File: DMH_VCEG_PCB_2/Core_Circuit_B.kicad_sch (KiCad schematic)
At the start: 84 parts, among them J25 Conn_01x10_PinHeader, Q5 BC548, Q6 BC558, Q7 BC548, SW2 SW_DPDT_x2, U10 TL074, U11 4001, U12 40106, U13 CD4066BE, U14 TL074, U15 TL074, U16 TL074

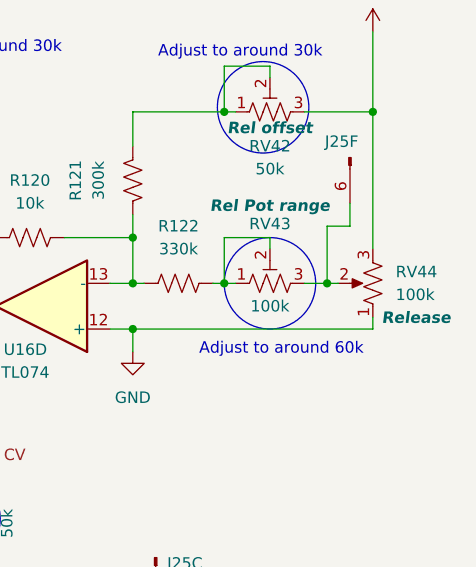
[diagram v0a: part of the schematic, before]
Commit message: Placed front panel components on PCB 2
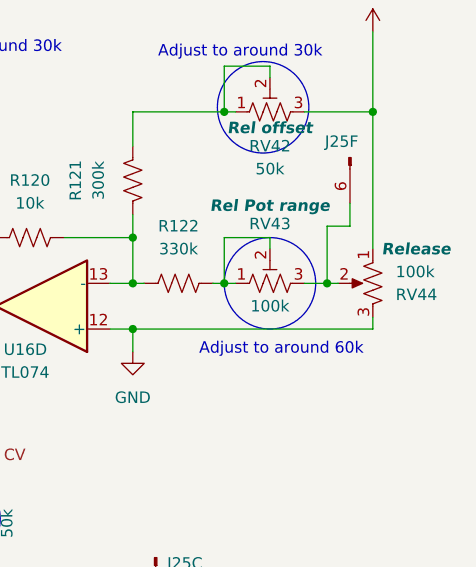
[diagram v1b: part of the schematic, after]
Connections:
- net +12V: now also RV44.1; no longer RV44.3
- net GND: now also RV44.3; no longer RV44.1
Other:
- moved on the sheet: RV44

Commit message: Placed ICs and pin headers on PCB 2
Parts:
- J25: footprint (none) -> Connector_PinSocket_2.54mm:PinSocket_1x10_P2.54mm_Vertical
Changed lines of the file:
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@@
 			)
 		)
-		(property "Footprint" ""
+		(property "Footprint" "Connector_PinSocket_2.54mm:PinSocket_1x10_P2.54mm_Vertical"
 			(at 184.15 139.7 0)
 			(effects
@@
 			)
 		)
-		(property "Footprint" ""
+		(property "Footprint" "Connector_PinSocket_2.54mm:PinSocket_1x10_P2.54mm_Vertical"
 			(at 273.05 33.02 0)
 			(effects
@@
 		(exclude_from_sim no)
 		(in_bom yes)
-		(on_board yes)
+		(on_board no)
 		(dnp no)
 		(property "Reference" "U10"
@@
 			)
 		)
-		(property "Footprint" ""
+		(property "Footprint" "Connector_PinSocket_2.54mm:PinSocket_1x10_P2.54mm_Vertical"
 			(at 127 157.48 0)
 			(effects
@@
 			)
 		)
-		(property "Footprint" ""
+		(property "Footprint" "Connector_PinSocket_2.54mm:PinSocket_1x10_P2.54mm_Vertical"
 			(at 151.13 189.23 0)
 			(effects
@@
 		(exclude_from_sim no)
 		(in_bom yes)
-		(on_board yes)
+		(on_board no)
 		(dnp no)
 		(property "Reference" "U10"
@@
 			)
 		)
-		(property "Footprint" ""
+		(property "Footprint" "Connector_PinSocket_2.54mm:PinSocket_1x10_P2.54mm_Vertical"
 			(at 251.46 77.47 0)
 			(effects

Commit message: Added Output attenuation circuit
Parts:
- RV34, RV40, RV44: value 100k -> C100k
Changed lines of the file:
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@@
 			)
 		)
-		(property "Value" "100k"
+		(property "Value" "C100k"
 			(at 132.08 166.3701 0)
 			(effects
@@
 			)
 		)
-		(property "Value" "100k"
+		(property "Value" "C100k"
 			(at 260.35 95.2499 0)
 			(effects
@@
 			)
 		)
-		(property "Value" "100k"
+		(property "Value" "C100k"
 			(at 278.13 45.7201 0)
 			(effects

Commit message: Removed unnecessary trimpots
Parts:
- removed RV31, RV37, RV38: 50k, Potentiometer_THT:Potentiometer_Bourns_3296W_Vertical, symbol Device:R_Potentiometer_Trim_US
- removed RV33, RV39, RV43: 100k, Potentiometer_THT:Potentiometer_Bourns_3296W_Vertical, symbol Device:R_Potentiometer_Trim_US
- R100, R119, R122: value 330k -> 390k
- R116, R118, R92: value 470k -> 499k
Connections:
- net Att CV: now also R118.2
- net Dec CV: now also R92.2
- net Rel CV: now also R116.2
- net at R122.1: now also J25.6 (Pin_6), RV44.2
- net at R100.1: now also J25.4 (Pin_4), RV34.2
- net at R119.1: now also J25.3 (Pin_3), RV40.2
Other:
- note removed: "Adjust to around 60k"
- moved on the sheet: R119, R122

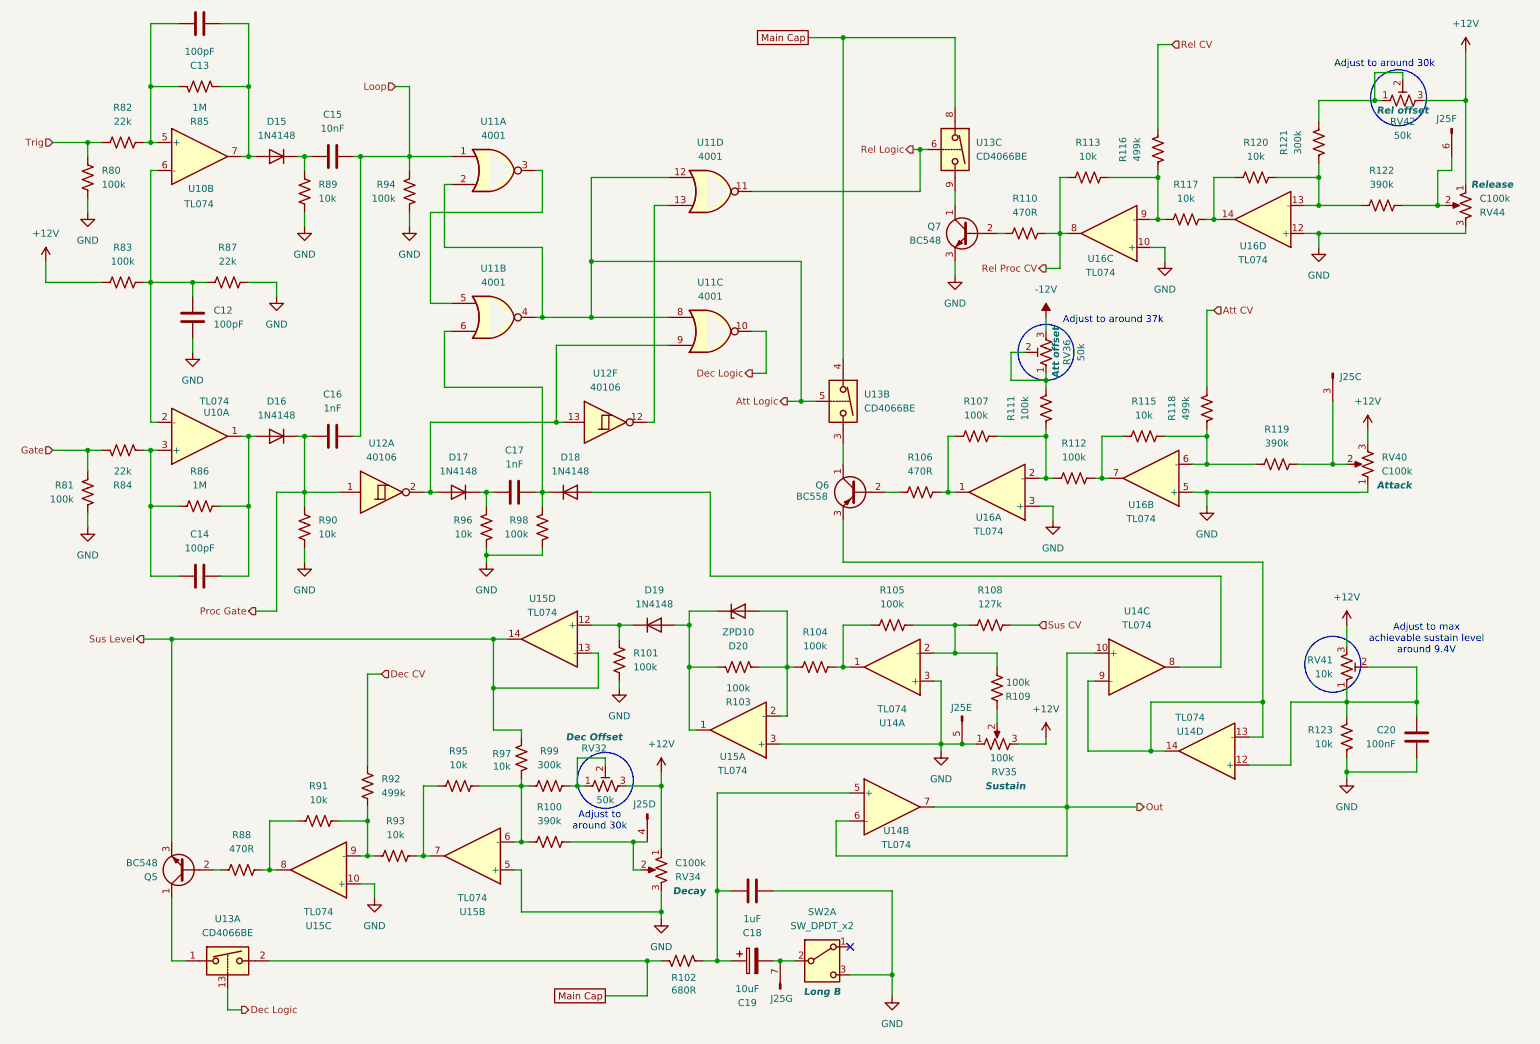
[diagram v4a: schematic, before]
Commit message: Synced PCB 2 project with PCB 1
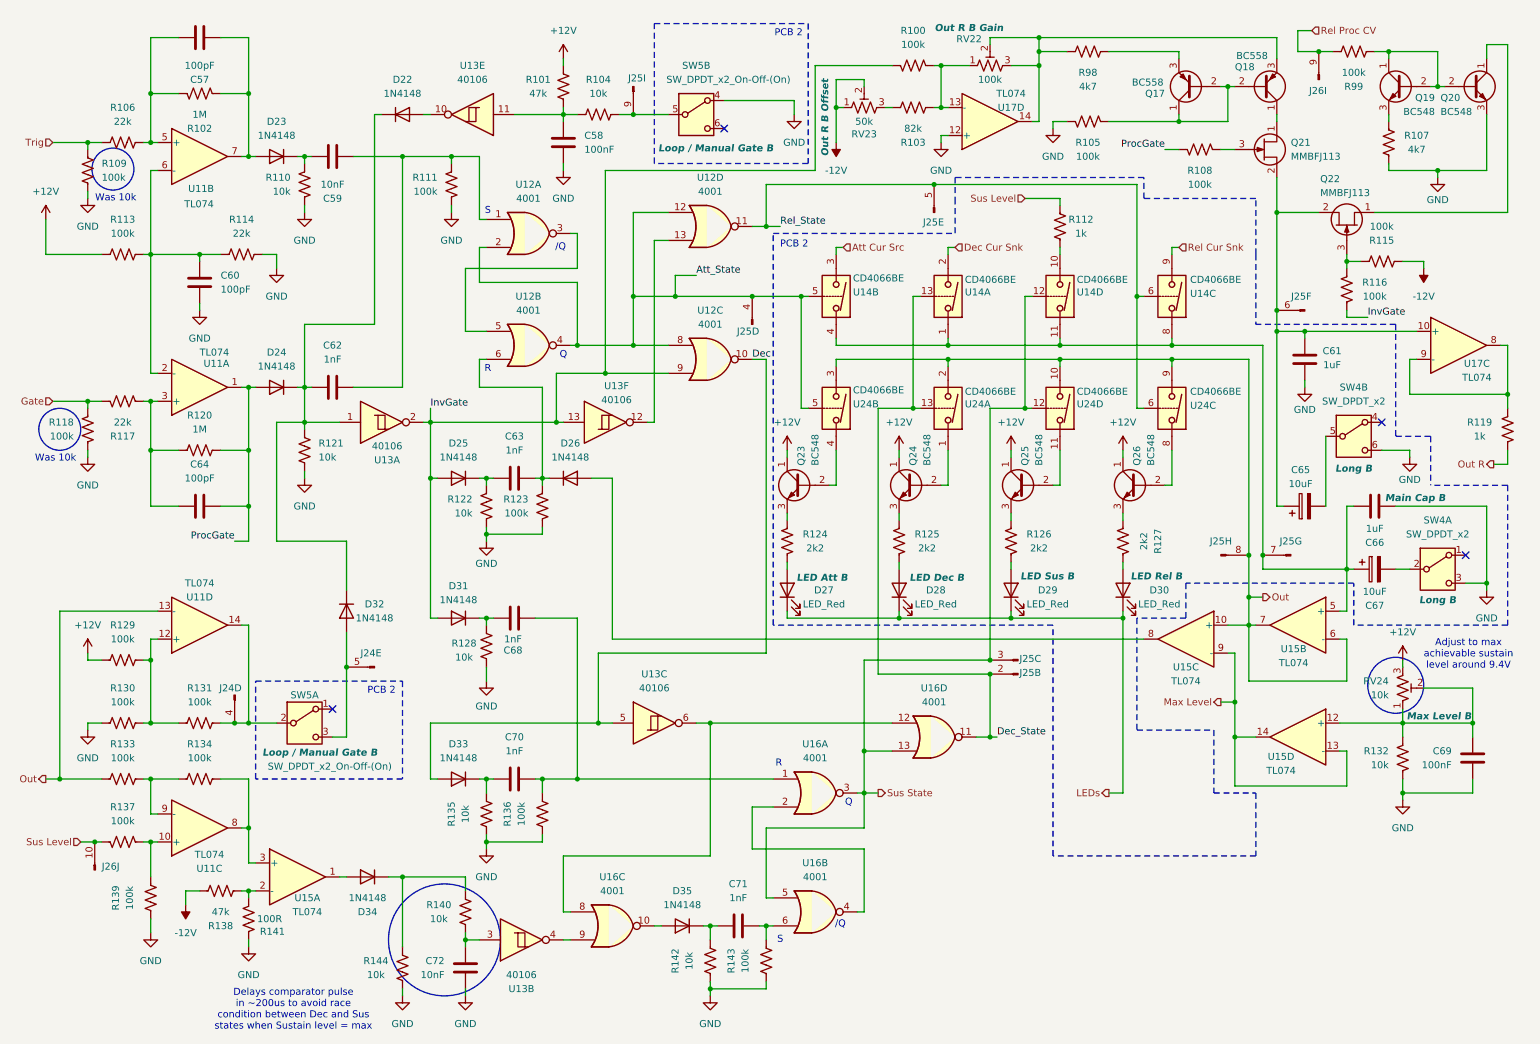
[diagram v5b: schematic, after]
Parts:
- removed C12, C13, C14: 100pF, Capacitor_THT:C_Disc_D3.8mm_W2.6mm_P2.50mm, symbol Device:C
- removed C15: 10nF, Capacitor_THT:C_Disc_D4.3mm_W1.9mm_P5.00mm, symbol Device:C
- removed C16, C17: 1nF, Capacitor_THT:C_Disc_D4.3mm_W1.9mm_P5.00mm, symbol Device:C
- removed C18: 1uF, Capacitor_THT:C_Disc_D4.3mm_W1.9mm_P5.00mm, symbol Device:C
- removed C19: 10uF, Capacitor_THT:CP_Radial_D5.0mm_P2.00mm, symbol Device:C_Polarized
- removed C20: 100nF, Capacitor_THT:C_Disc_D4.3mm_W1.9mm_P5.00mm, symbol Device:C
- removed D15, D16, D17, D18, D19: 1N4148, Diode_THT:D_DO-35_SOD27_P7.62mm_Horizontal, symbol Diode:1N4148
- removed D20: ZPD10, Diode_THT:D_DO-35_SOD27_P7.62mm_Horizontal, symbol Diode:ZPDxx
- removed Q5, Q7: BC548, Package_TO_SOT_THT:TO-92L_Inline_Wide, symbol Transistor_BJT:BC548
- removed Q6: BC558, Package_TO_SOT_THT:TO-92L_Inline_Wide, symbol Transistor_BJT:BC558
- removed R80, R81, R83, R94: 100k, Resistor_THT:R_Axial_DIN0207_L6.3mm_D2.5mm_P7.62mm_Horizontal, symbol Device:R_US
- removed R82, R84, R87: 22k, Resistor_THT:R_Axial_DIN0207_L6.3mm_D2.5mm_P7.62mm_Horizontal, symbol Device:R_US
- removed R85, R86: 1M, Resistor_THT:R_Axial_DIN0207_L6.3mm_D2.5mm_P7.62mm_Horizontal, symbol Device:R_US
- removed R88: 470R, Resistor_THT:R_Axial_DIN0207_L6.3mm_D2.5mm_P7.62mm_Horizontal, symbol Device:R_US
- removed R89, R90, R91, R93, R95, R96, R97: 10k, Resistor_THT:R_Axial_DIN0207_L6.3mm_D2.5mm_P7.62mm_Horizontal, symbol Device:R_US
- removed R92: 499k, Resistor_THT:R_Axial_DIN0207_L6.3mm_D2.5mm_P7.62mm_Horizontal, symbol Device:R_US
- removed RV32, RV36, RV42: 50k, Potentiometer_THT:Potentiometer_Bourns_3296W_Vertical, symbol Device:R_Potentiometer_Trim_US
- removed RV34, RV40, RV44: C100k, SynthStuff:Potentiometer_Alpha_RD901F-40-00D_Single_Vertical, symbol Device:R_Potentiometer_US
- removed RV35: 100k, SynthStuff:Potentiometer_Alpha_RD901F-40-00D_Single_Vertical, symbol Device:R_Potentiometer_US
- removed RV41: 10k, Potentiometer_THT:Potentiometer_Bourns_3296W_Vertical, symbol Device:R_Potentiometer_Trim_US
- removed SW2: SW_DPDT_x2, SynthStuff:Toggle_Switch_2_Poles_TE, symbol Switch:SW_DPDT_x2
- removed U10, U14, U16: TL074, Package_DIP:DIP-14_W7.62mm_Socket, symbol Amplifier_Operational:TL074
- removed U11: 4001, Package_DIP:DIP-14_W7.62mm_Socket, symbol 4xxx:4001
- removed U12: 40106, Package_DIP:DIP-14_W7.62mm_Socket, symbol 4xxx:40106
- removed U13: CD4066BE, Package_DIP:DIP-14_W7.62mm, symbol Analog_Switch:CD4066BE
- added C57, C60, C64: 100pF, Capacitor_THT:C_Disc_D3.8mm_W2.6mm_P2.50mm, symbol Device:C
- added C58, C69: 100nF, Capacitor_THT:C_Disc_D4.3mm_W1.9mm_P5.00mm, symbol Device:C
- added C59, C72: 10nF, Capacitor_THT:C_Disc_D4.3mm_W1.9mm_P5.00mm, symbol Device:C
- added C61, C66: 1uF, Capacitor_THT:C_Rect_L7.0mm_W4.5mm_P5.00mm, symbol Device:C
- added C62, C63, C68, C70, C71: 1nF, Capacitor_THT:C_Disc_D4.3mm_W1.9mm_P5.00mm, symbol Device:C
- added C65, C67: 10uF, Capacitor_THT:CP_Radial_D4.0mm_P1.50mm, symbol Device:C_Polarized
- added D22, D23, D24, D25, D26, D31, D32, D33, D34, D35: 1N4148, Diode_THT:D_DO-35_SOD27_P7.62mm_Horizontal, symbol Diode:1N4148
- added D27, D28, D29, D30: LED_Red, LED_THT:LED_D3.0mm, symbol Device:LED
- added J24: Conn_01x06_PinHeader, Connector_PinHeader_2.54mm:PinHeader_1x06_P2.54mm_Vertical, symbol SynthStuff:Conn_01x06_PinHeader
- added unit 2 of J25
- added unit 9 of J25
- added unit 8 of J25
- added J26: Conn_01x10_PinHeader, Connector_PinSocket_2.54mm:PinSocket_1x10_P2.54mm_Vertical, symbol SynthStuff:Conn_01x10_PinHeader
- added Q17, Q18: BC558, Package_TO_SOT_THT:TO-92L_Inline_Wide, symbol Transistor_BJT:BC558
- added Q19, Q20, Q23, Q24, Q25, Q26: BC548, Package_TO_SOT_THT:TO-92L_Inline_Wide, symbol Transistor_BJT:BC548
- added Q21, Q22: MMBFJ113, Package_TO_SOT_THT:TO-92L_Inline, symbol Transistor_FET:MMBFJ113
- added R114: 22k, Resistor_THT:R_Axial_DIN0207_L6.3mm_D2.5mm_P7.62mm_Horizontal, symbol Device:R_US
- added R124, R125, R126, R127: 2k2, Resistor_THT:R_Axial_DIN0207_L6.3mm_D2.5mm_P7.62mm_Horizontal, symbol Device:R_US
- added R128, R132, R135, R140, R142, R144: 10k, Resistor_THT:R_Axial_DIN0207_L6.3mm_D2.5mm_P7.62mm_Horizontal, symbol Device:R_US
- added R129, R130, R131, R133, R134, R136, R137, R139, R143: 100k, Resistor_THT:R_Axial_DIN0207_L6.3mm_D2.5mm_P7.62mm_Horizontal, symbol Device:R_US
- added R138: 47k, Resistor_THT:R_Axial_DIN0207_L6.3mm_D2.5mm_P7.62mm_Horizontal, symbol Device:R_US
- added R141: 100R, Resistor_THT:R_Axial_DIN0207_L6.3mm_D2.5mm_P7.62mm_Horizontal, symbol Device:R_US
- added RV22: 100k, Potentiometer_THT:Potentiometer_Bourns_3296W_Vertical, symbol Device:R_Potentiometer_Trim_US
- added RV23: 50k, Potentiometer_THT:Potentiometer_Bourns_3296W_Vertical, symbol Device:R_Potentiometer_Trim_US
- added RV24: 10k, Potentiometer_THT:Potentiometer_Bourns_3296W_Vertical, symbol Device:R_Potentiometer_Trim_US
- added SW4: SW_DPDT_x2, SynthStuff:Toggle_Switch_2_Poles_TE, symbol Switch:SW_DPDT_x2
- added SW5: SW_DPDT_x2_On-Off-(On), SynthStuff:Toggle_Switch_2_Poles_TE, symbol Switch:SW_DPDT_x2
- added U11, U17: TL074, Package_DIP:DIP-14_W7.62mm_Socket, symbol Amplifier_Operational:TL074
- added U12, U16: 4001, Package_DIP:DIP-14_W7.62mm_Socket, symbol 4xxx:4001
- added U13: 40106, Package_DIP:DIP-14_W7.62mm_Socket, symbol 4xxx:40106
- added U14, U24: CD4066BE, Package_DIP:DIP-14_W7.62mm, symbol Analog_Switch:CD4066BE
- J25: footprint Connector_PinSocket_2.54mm:PinSocket_1x10_P2.54mm_Vertical -> Connector_PinHeader_2.54mm:PinHeader_1x10_P2.54mm_Vertical
- R100: value 390k -> 100k
- R101: value 100k -> 47k
- R102: value 680R -> 1M
- R103: value 100k -> 82k
- R104: value 100k -> 10k
- R106: value 470R -> 22k
- R107, R98: value 100k -> 4k7
- R108: value 127k -> 100k
- R110: value 470R -> 10k
- R112: value 100k -> 1k
- R113, R115, R123: value 10k -> 100k
- R116, R118: value 499k -> 100k
- R117: value 10k -> 22k
- R119: value 390k -> 1k
- R120: value 10k -> 1M
- R121: value 300k -> 10k
- R122: value 390k -> 10k
- R99: value 300k -> 100k
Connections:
- net Att CV is gone; now on net Gate: R118.2
- net +12V: now also R101.1, R113.2, Q23.1 (C), Q24.1 (C), Q25.1 (C), Q26.1 (C), R129.2, RV24.3
- net -12V: now also R115.1, R138.1, RV23.1, RV23.2
- net GND: now also R105.2, R107.1, R109.1, R110.1, R111.1, R118.1, R121.1, R122.1, C58.2, C60.1, C61.1, C66.2, C69.1, C72.1, Q20.3 (E), R114.1, R128.2, R130.2, R132.1, R135.2, R136.2, R139.2, R141.2, R142.2, R143.2, R144.2, SW4.3 (C), SW4.6 (C), SW5.4 (A), U17.12 (+); no longer J25.5 (Pin_5), R101.1, R98.1, U15.10 (+), U15.3 (+), U15.5 (+)
- net Gate: now also R117.2
- net Out: now also U15.10 (+), U15.6 (-), U15.7, J25.8 (Pin_8), R133.2, U11.13 (-), U24.10, U24.2, U24.3, U24.9
- net Rel Proc CV: now also R99.1, J26.9 (Pin_9); no longer R110.1, R113.2
- net Sus Level: now also R112.2, J26.10 (Pin_10), R137.1; no longer U15.13 (-), U15.14
- net Trig: now also R106.2, R109.2
- net at R123.2: now also C63.2, D26.1 (K), U12.6
- net Att_State: now reaches J25.4 (Pin_4)
- net Att_State: now also U12.12, U12.2, U12.4, U12.8, U14.5, U24.5; no longer R100.1
- net at R102.1: now also C57.2, D23.2 (A), U11.7
- net Max Level: now reaches U15.9 (-)
- net Max Level: now also U15.13 (-), U15.14
- net at R107.2: now also Q19.3 (E); no longer R106.1
- net at R110.2: now also C59.1, D23.1 (K)
- net at U15.8: now also D26.2 (A)
- net at J25.6 (Pin_6): now also C61.2, C65.1, Q21.2 (S), Q22.2 (S), U17.10 (+); no longer R122.1
- net at R115.2: now also R116.1, Q22.3 (G); no longer R112.1
- net at R101.2: now also R104.2, C58.1, U13.11; no longer U15.12 (+)
- net at R103.2: now also R100.2, RV22.1, U17.13 (-); no longer U15.1
- net at R98.2: now also Q17.3 (E)
- net at R121.2: now also C62.1, D22.1 (K), D24.1 (K), D32.1 (K), U13.1
- net at J25.7 (Pin_7): now also U15.5 (+), C66.1, C67.1, U14.1, U14.11, U14.4, U14.8
- net at R111.2: now also C59.2, C62.2, U12.1
- net at R117.1, R120.2: now also C64.1, U11.3 (+)
- net at R104.1: now also J25.9 (Pin_9), SW5.5 (B); no longer R105.2
- net Out R: now reaches R119.1
- net Out R: no longer J25.3 (Pin_3)
- net Main Cap: no longer names the net of R102.2
- net Main Cap: now also R106.1, C57.1, U11.5 (+)
- net Rel CV renamed InvGate
- net InvGate: now also R100.1, D25.2 (A), D31.2 (A), U12.9, U13.13, U13.2
- net Sus CV: no longer names the net of R108.1
- net Sus CV: now also Q21.3 (G)
- new net: Q23.2 (B), U24.4
- new net: Q26.3 (E), R127.1
- new net: D30.2 (A), R127.2
- new net: D32.2 (A), J24.5 (Pin_5), SW5.3 (C)
- new net: C63.1, D25.1 (K), R122.2
- new net: Q25.2 (B), U24.11
- new net: C65.2, SW4.5 (B)
- new net: C60.2, R113.1, R114.2, U11.2 (-), U11.6 (-)
- new net: Q20.1 (C), Q22.1 (D)
- new net: Q26.2 (B), U24.8
- new net: R137.2, R139.1, U11.10 (+)
- new net: R134.1, U11.8, U15.3 (+)
- new net: R133.1, R134.2, U11.9 (-)
- new net: D22.2 (A), U13.10
- new net: U12.3, U12.5
- new net: Q25.3 (E), R126.1
- new net: Q23.3 (E), R124.1
- new net: D27.2 (A), R124.2
- new net: U12.13, U13.12
- new net: Q18.1 (C), Q21.1 (D)
- new net: C69.2, R132.2, RV24.1, RV24.2, U15.12 (+)
- new net: Q19.1 (C), Q19.2 (B), Q20.2 (B), R99.2
- new net: Q24.3 (E), R125.1
- new net: D28.2 (A), R125.2
- new net: Q18.3 (E), R98.1, RV22.2, RV22.3, U17.14
- new net: R112.1, U14.10
- new net: C68.1, D31.1 (K), R128.1
- new net: C68.2, C70.2, R136.1, U16.1
- new net: U13.6, U16.12, U16.8
- new net: D29.2 (A), R126.2
- new net: J24.4 (Pin_4), R131.1, SW5.2 (B), U11.14
- new net: D34.2 (A), U15.1
- new net: R138.2, R141.1, U15.2 (-)
- new net: C71.1, D35.1 (K), R142.1
- new net: Q17.1 (C), Q17.2 (B), Q18.2 (B), R105.1
- new net: C70.1, D33.1 (K), R135.1
- new net: U16.2, U16.4
- new net: D35.2 (A), U16.10
- new net: U13.4, U16.9
- new net: R119.2, U17.8, U17.9 (-)
- new net: R129.1, R130.1, R131.2, U11.12 (+)
- new net: D34.1 (K), R140.1, R144.1
- new net: C72.2, R140.2, U13.3
- new net: C67.2, SW4.2 (B)
- new net: C71.2, R143.1, U16.6
- new net: Q24.2 (B), U24.1
- new net: R103.1, RV23.3
- new net Att Cur Src: U14.3
- new net Dec: D33.2 (A), U12.10, U13.5
- new net Dec Cur Snk: U14.2
- new net Dec_State: J25.2 (Pin_2), U14.13, U16.11, U24.13
- new net LEDs: D27.1 (K), D28.1 (K), D29.1 (K), D30.1 (K)
- new net ProcGate: C64.2, D24.2 (A), R108.2, R120.1, U11.1
- new net Rel Cur Snk: U14.9
- new net Rel_State: J25.5 (Pin_5), U12.11, U14.6, U24.6
- new net Sus State: J25.3 (Pin_3), U14.12, U16.13, U16.3, U16.5, U24.12
- no-connect marks 1 -> 4
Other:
- note added: "/Q"
- note added: "Delays comparator pulse in ~200us to avoid race condition between Dec and Sus states when Sustain level = max"
- note added: "PCB 2"
- note added: "Q"
- note added: "R"
- note added: "S"
- note added: "Was 10k"
- note removed: "Adjust to around 30k"
- note removed: "Adjust to around 37k"

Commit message: Started placement on PCB 2
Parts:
- J24: footprint Connector_PinHeader_2.54mm:PinHeader_1x06_P2.54mm_Vertical -> Connector_PinSocket_2.54mm:PinSocket_1x06_P2.54mm_Vertical
- J25: footprint Connector_PinHeader_2.54mm:PinHeader_1x10_P2.54mm_Vertical -> Connector_PinSocket_2.54mm:PinSocket_1x10_P2.54mm_Vertical
- U14, U24: footprint Package_DIP:DIP-14_W7.62mm -> Package_DIP:DIP-14_W7.62mm_Socket
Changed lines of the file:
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@@
 			)
 		)
-		(property "Footprint" "Package_DIP:DIP-14_W7.62mm"
+		(property "Footprint" "Package_DIP:DIP-14_W7.62mm_Socket"
 			(at 158.75 83.82 0)
 			(effects
@@
 			)
 		)
-		(property "Footprint" "Package_DIP:DIP-14_W7.62mm"
+		(property "Footprint" "Package_DIP:DIP-14_W7.62mm_Socket"
 			(at 199.39 83.82 0)
 			(effects
@@
 			)
 		)
-		(property "Footprint" "Package_DIP:DIP-14_W7.62mm"
+		(property "Footprint" "Package_DIP:DIP-14_W7.62mm_Socket"
 			(at 219.71 83.82 0)
 			(effects
@@
 			)
 		)
-		(property "Footprint" "Connector_PinHeader_2.54mm:PinHeader_1x10_P2.54mm_Vertical"
+		(property "Footprint" "Connector_PinSocket_2.54mm:PinSocket_1x10_P2.54mm_Vertical"
 			(at 179.07 48.26 0)
 			(effects
@@
 			)
 		)
-		(property "Footprint" "Connector_PinHeader_2.54mm:PinHeader_1x06_P2.54mm_Vertical"
+		(property "Footprint" "Connector_PinSocket_2.54mm:PinSocket_1x06_P2.54mm_Vertical"
 			(at 77.47 130.81 0)
 			(effects
@@
 			)
 		)
-		(property "Footprint" "Package_DIP:DIP-14_W7.62mm"
+		(property "Footprint" "Package_DIP:DIP-14_W7.62mm_Socket"
 			(at 158.75 63.5 0)
 			(effects
@@
 			)
 		)
-		(property "Footprint" "Connector_PinHeader_2.54mm:PinHeader_1x06_P2.54mm_Vertical"
+		(property "Footprint" "Connector_PinSocket_2.54mm:PinSocket_1x06_P2.54mm_Vertical"
 			(at 52.07 135.89 0)
 			(effects
@@
 			)
 		)
-		(property "Footprint" "Connector_PinHeader_2.54mm:PinHeader_1x10_P2.54mm_Vertical"
+		(property "Footprint" "Connector_PinSocket_2.54mm:PinSocket_1x10_P2.54mm_Vertical"
 			(at 194.31 132.08 0)
 			(effects
@@
 			)
 		)
-		(property "Footprint" "Connector_PinHeader_2.54mm:PinHeader_1x10_P2.54mm_Vertical"
+		(property "Footprint" "Connector_PinSocket_2.54mm:PinSocket_1x10_P2.54mm_Vertical"
 			(at 194.31 129.54 0)
 			(effects
@@
 			)
 		)
-		(property "Footprint" "Package_DIP:DIP-14_W7.62mm"
+		(property "Footprint" "Package_DIP:DIP-14_W7.62mm_Socket"
 			(at 179.07 63.5 0)
 			(effects
@@
 			)
 		)
-		(property "Footprint" "Connector_PinHeader_2.54mm:PinHeader_1x10_P2.54mm_Vertical"
+		(property "Footprint" "Connector_PinSocket_2.54mm:PinSocket_1x10_P2.54mm_Vertical"
 			(at 124.46 25.4 0)
 			(effects
@@
 			)
 		)
-		(property "Footprint" "Package_DIP:DIP-14_W7.62mm"
+		(property "Footprint" "Package_DIP:DIP-14_W7.62mm_Socket"
 			(at 219.71 63.5 0)
 			(effects
@@
 			)
 		)
-		(property "Footprint" "Package_DIP:DIP-14_W7.62mm"
+		(property "Footprint" "Package_DIP:DIP-14_W7.62mm_Socket"
 			(at 179.07 83.82 0)
 			(effects
@@
 			)
 		)
-		(property "Footprint" "Connector_PinHeader_2.54mm:PinHeader_1x10_P2.54mm_Vertical"
+		(property "Footprint" "Connector_PinSocket_2.54mm:PinSocket_1x10_P2.54mm_Vertical"
 			(at 146.05 68.58 0)
 			(effects
@@
 			)
 		)
-		(property "Footprint" "Connector_PinHeader_2.54mm:PinHeader_1x10_P2.54mm_Vertical"
+		(property "Footprint" "Connector_PinSocket_2.54mm:PinSocket_1x10_P2.54mm_Vertical"
 			(at 246.38 66.04 0)
 			(effects
@@
 			)
 		)
-		(property "Footprint" "Connector_PinHeader_2.54mm:PinHeader_1x10_P2.54mm_Vertical"
+		(property "Footprint" "Connector_PinSocket_2.54mm:PinSocket_1x10_P2.54mm_Vertical"
 			(at 231.14 110.49 0)
 			(effects
@@
 			)
 		)
-		(property "Footprint" "Package_DIP:DIP-14_W7.62mm"
+		(property "Footprint" "Package_DIP:DIP-14_W7.62mm_Socket"
 			(at 199.39 63.5 0)
 			(effects
@@
 			)
 		)
-		(property "Footprint" "Connector_PinHeader_2.54mm:PinHeader_1x10_P2.54mm_Vertical"
+		(property "Footprint" "Connector_PinSocket_2.54mm:PinSocket_1x10_P2.54mm_Vertical"
 			(at 243.84 110.49 0)
 			(effects
